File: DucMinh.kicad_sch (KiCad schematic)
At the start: 51 parts, among them J5 USB_B_Micro, J8 Conn_01x04, SW1 SW_Push, U1 STM32F103C8T6, U2 AMS1117-3.3, U3 LM2596SX-5.0/NOPB, U4 TMC2209_SILENTSTEPSTICK, Y1 8 MHz, Y3 32.768 kHz

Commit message: fix routes
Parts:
- removed C11: 10uF, Capacitor_SMD:C_1206_3216Metric_Pad1.33x1.80mm_HandSolder, symbol Device:C
- added C11: 10uf, ul_tantalum6032:tue_tantalum_6032, symbol Device:C_Polarized_US
- R2: footprint Capacitor_SMD:C_0603_1608Metric_Pad1.08x0.95mm_HandSolder -> Resistor_SMD:R_0603_1608Metric_Pad0.98x0.95mm_HandSolder
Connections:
- net +3V3: now also C11.1
- net GND: now also C11.2
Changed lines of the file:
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@@
 	)
 	(symbol
+		(lib_id "Device:C_Polarized_US")
+		(at 127 196.85 0)
+		(unit 1)
+		(exclude_from_sim no)
+		(in_bom yes)
+		(on_board yes)
+		(dnp no)
+		(fields_autoplaced yes)
+		(property "Reference" "C11"
+			(at 130.81 194.9449 0)
+			(effects
+				(font
+					(size 1.27 1.27)
+				)
+				(justify left)
+			)
+		)
+		(property "Value" "10uf"
+			(at 130.81 197.4849 0)
+			(effects
+				(font
+					(size 1.27 1.27)
+				)
+				(justify left)
+			)
+		)
+		(property "Footprint" "ul_tantalum6032:tue_tantalum_6032"
+			(at 127 196.85 0)
+			(effects
+				(font
+					(size 1.27 1.27)
+				)
+				(hide yes)
+			)
+		)
+		(property "Datasheet" "~"
+			(at 127 196.85 0)
+			(effects
+				(font
+					(size 1.27 1.27)
+				)
+				(hide yes)
+			)
+		)
+		(property "Description" "Polarized capacitor, US symbol"
+			(at 127 196.85 0)
+			(effects
+				(font
+					(size 1.27 1.27)
+				)
+				(hide yes)
+			)
+		)
+		(pin "1"
+		)
+		(pin "2"
+		)
+		(instances
+			(project "DucMinh"
+				(path "/e454eeda-a1de-43c9-95d8-58adcb0266a5"
+					(reference "C11")
+					(unit 1)
+				)
+			)
+		)
+	)
+	(symbol
 		(lib_id "power:VDC")
 		(at 220.98 152.4 0)
@@
 	)
 	(symbol
-		(lib_id "Device:C")
-		(at 127 196.85 0)
-		(unit 1)
-		(exclude_from_sim no)
-		(in_bom yes)
-		(on_board yes)
-		(dnp no)
-		(fields_autoplaced yes)
-		(property "Reference" "C11"
-			(at 130.81 195.5799 0)
-			(effects
-				(font
-					(size 1.27 1.27)
-				)
-				(justify left)
-			)
-		)
-		(property "Value" "10uF"
-			(at 130.81 198.1199 0)
-			(effects
-				(font
-					(size 1.27 1.27)
-				)
-				(justify left)
-			)
-		)
-		(property "Footprint" "Capacitor_SMD:C_1206_3216Metric_Pad1.33x1.80mm_HandSolder"
-			(at 127.9652 200.66 0)
-			(effects
-				(font
-					(size 1.27 1.27)
-				)
-				(hide yes)
-			)
-		)
-		(property "Datasheet" "~"
-			(at 127 196.85 0)
-			(effects
-				(font
-					(size 1.27 1.27)
-				)
-				(hide yes)
-			)
-		)
-		(property "Description" "Unpolarized capacitor"
-			(at 127 196.85 0)
-			(effects
-				(font
-					(size 1.27 1.27)
-				)
-				(hide yes)
-			)
-		)
-		(pin "1"
-		)
-		(pin "2"
-		)
-		(instances
-			(project "UART_Half_Duplex"
-				(path "/e454eeda-a1de-43c9-95d8-58adcb0266a5"
-					(reference "C11")
-					(unit 1)
-				)
-			)
-		)
-	)
-	(symbol
 		(lib_id "power:GND")
 		(at 85.09 264.16 270)
@@
 			)
 		)
-		(property "Footprint" "Capacitor_SMD:C_0603_1608Metric_Pad1.08x0.95mm_HandSolder"
+		(property "Footprint" "Resistor_SMD:R_0603_1608Metric_Pad0.98x0.95mm_HandSolder"
 			(at 375.92 83.312 90)
 			(effects

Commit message: .
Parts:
- removed BOOT1: BOOT1, ul_switch-SS12D00:tue_SS12D00_3P_2.5mm, symbol Connector_Generic:Conn_01x03
- removed C15, C16: 10pf, Capacitor_SMD:C_0603_1608Metric_Pad1.08x0.95mm_HandSolder, symbol Device:C
- removed SWD1: SWD, Connector_PinHeader_2.54mm:PinHeader_1x03_P2.54mm_Vertical, symbol Connector_Generic:Conn_01x03
- removed Y3: 32.768 kHz, ul_crytsal_mc306:SOJ_MC-306_EPS, symbol Device:Crystal_GND23
- added STLink_EN1: POWER, Connector_PinHeader_2.54mm:PinHeader_1x02_P2.54mm_Vertical, symbol Connector_Generic:Conn_01x02
- added SWD1: Conn_01x04, Connector_JST:JST_XH_B4B-XH-A_1x04_P2.50mm_Vertical, symbol Connector_Generic:Conn_01x04
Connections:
- net BOOT1 is gone; now on net GND: R7.1
- net +3V3: now also STLink_EN1.1 (Pin_1)
- net GND: now also SWD1.4 (Pin_4)
- net SWD_CLK: now also SWD1.3 (Pin_3)
- net SWD_IO: now also SWD1.2 (Pin_2)
- net 5V_Drive: now reaches PWM1.1-3
- net 5V_Drive: now also PWM1.2-3, PWM1.3-3
- net LSE_OCS_IN: no longer names the net of U1.3 (PC14-OSC32_IN)
- net LSE_OCS_OUT: no longer names the net of U1.4 (PC15-OSC32_OUT)
- new net 3V3_STLINK: STLink_EN1.2 (Pin_2), SWD1.1 (Pin_1)
- no-connect marks 15 -> 10
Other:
- moved on the sheet: C13, C14, R5, R7, R8, TMC_EN1, U1A, Y1

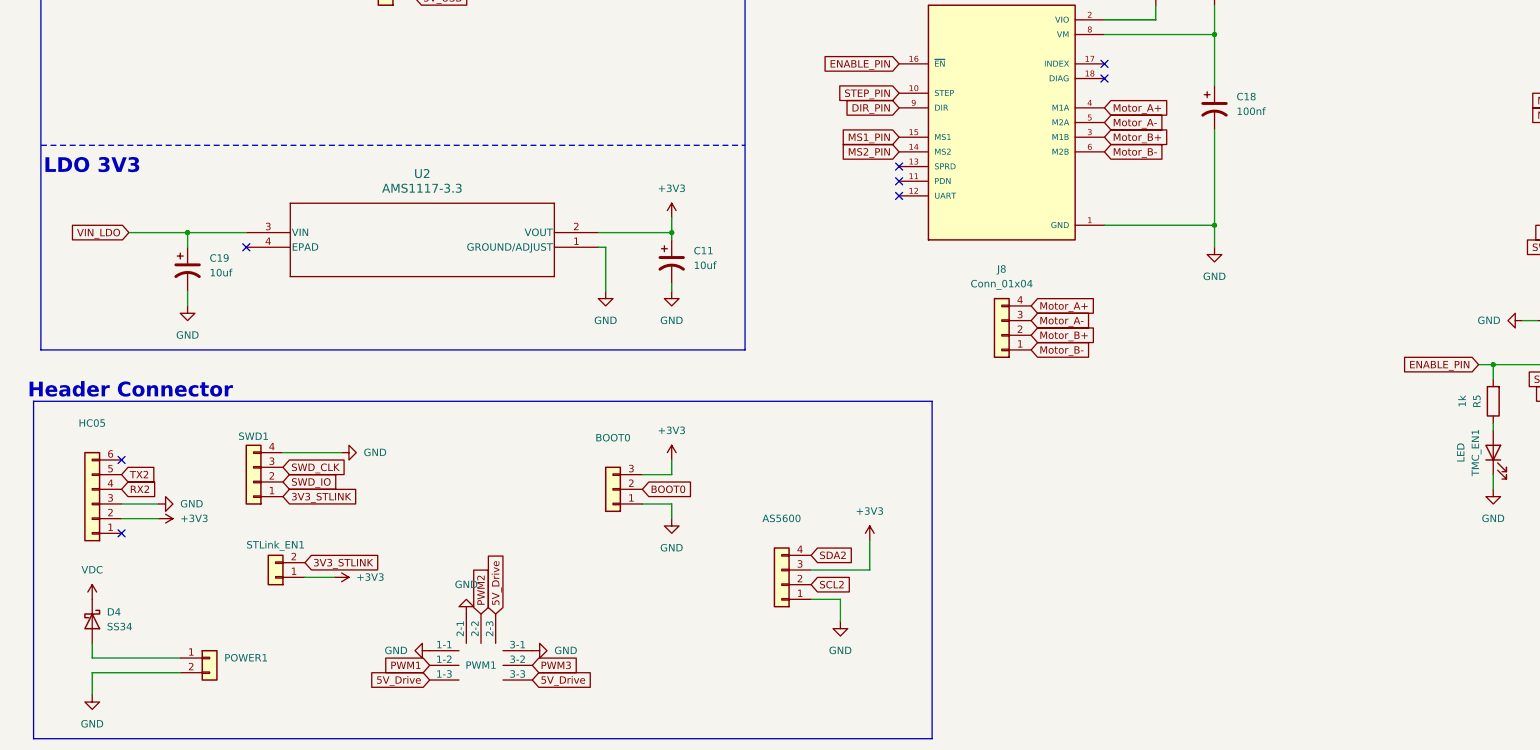
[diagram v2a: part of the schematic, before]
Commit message: add 74hct125 routes
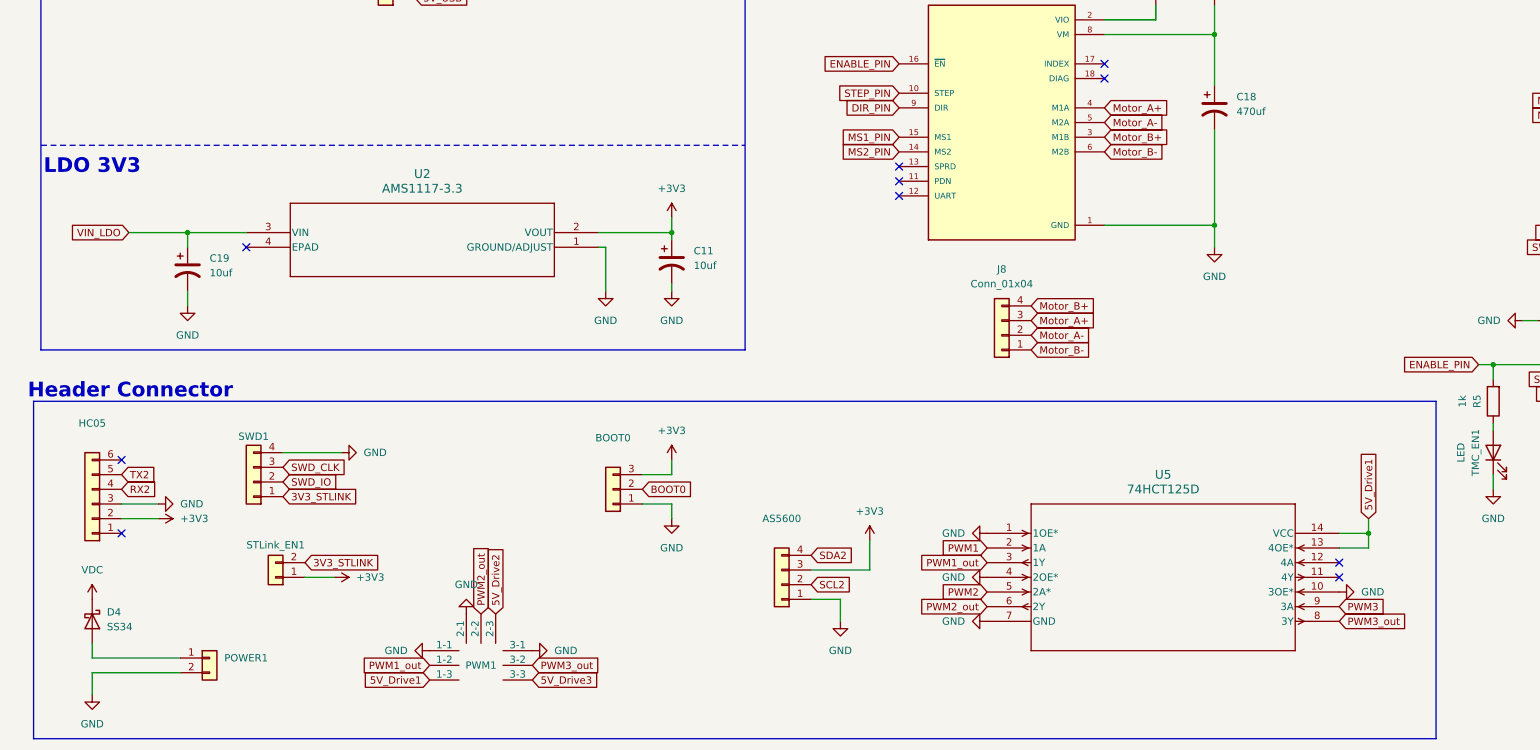
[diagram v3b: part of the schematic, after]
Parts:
- added U5: 74HCT125D, tue_74hct125:SOT108-1_NXP, symbol tue_74hct125d:74HCT125D
- C18: value 100nf -> 470uf
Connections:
- net GND: now also U5.1 (1OE*), U5.10 (3OE*), U5.4 (2OE*), U5.7 (GND)
- net Motor_A+: now also J8.3 (Pin_3); no longer J8.4 (Pin_4)
- net Motor_A-: now also J8.2 (Pin_2); no longer J8.3 (Pin_3)
- net Motor_B+: now also J8.4 (Pin_4); no longer J8.2 (Pin_2)
- net PWM1: now also U5.2 (1A); no longer PWM1.1-2
- net PWM2: now also U5.5 (2A*); no longer PWM1.2-2
- net PWM3: now also U5.9 (3A); no longer PWM1.3-2
- removed net 5V_Drive: PWM1.1-3, PWM1.2-3, PWM1.3-3
- new net 5V_Drive1: PWM1.1-3, U5.13 (4OE*), U5.14 (VCC)
- new net 5V_Drive2: PWM1.2-3
- new net 5V_Drive3: PWM1.3-3
- new net PWM1_out: PWM1.1-2, U5.3 (1Y)
- new net PWM2_out: PWM1.2-2, U5.6 (2Y)
- new net PWM3_out: PWM1.3-2, U5.8 (3Y)
- no-connect marks 10 -> 12

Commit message: add bts7960
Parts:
- removed AS5600: AS5600, Connector_PinHeader_2.54mm:PinHeader_1x04_P2.54mm_Vertical, symbol Connector_Generic:Conn_01x04
- removed BOOT0: BOOT0, ul_switch-SS12D00:tue_SS12D00_3P_2.5mm, symbol Connector_Generic:Conn_01x03
- removed C13: 20pf, Capacitor_SMD:C_0603_1608Metric_Pad1.08x0.95mm_HandSolder, symbol Device:C
- removed C5: 10uf, Capacitor_SMD:C_0603_1608Metric_Pad1.08x0.95mm_HandSolder, symbol Device:C
- removed C8: 1uf, Capacitor_SMD:C_0603_1608Metric_Pad1.08x0.95mm_HandSolder, symbol Device:C
- removed HC05: HC05, Connector_PinHeader_2.54mm:PinHeader_1x06_P2.54mm_Vertical, symbol Connector_Generic:Conn_01x06
- removed PC13, PWR1, TMC_EN1: LED, LED_SMD:LED_0603_1608Metric_Pad1.05x0.95mm_HandSolder, symbol Device:LED
- removed POWER1: POWER, ul_TerminalBlock:TerminalBlock_bornier-2_P5.08mm, symbol Connector_Generic:Conn_01x02
- removed PWM1: ~, ul_Conn_03x03:tue_conn_03x03_2.54mm, symbol Conn_03x03:Conn_03x03
- removed R2, R4, R5: 1k, Resistor_SMD:R_0603_1608Metric_Pad0.98x0.95mm_HandSolder, symbol Device:R
- removed R8: 10k, Resistor_SMD:R_0603_1608Metric_Pad0.98x0.95mm_HandSolder, symbol Device:R
- removed STLink_EN1: POWER, Connector_PinHeader_2.54mm:PinHeader_1x02_P2.54mm_Vertical, symbol Connector_Generic:Conn_01x02
- removed SWD1: Conn_01x04, Connector_JST:JST_XH_B4B-XH-A_1x04_P2.50mm_Vertical, symbol Connector_Generic:Conn_01x04
- removed U1: STM32F103C8T6, ul_stm32:LQFP48_STM, symbol ul_STM32F103C8T6:STM32F103C8T6
- removed U5: 74HCT125D, tue_74hct125:SOT108-1_NXP, symbol tue_74hct125d:74HCT125D
- removed VIN1: Conn_01x03, ul_switch-SS12D00:tue_SS12D00_3P_2.5mm, symbol Connector_Generic:Conn_01x03
- added C11, C12, C13: 330uf, Capacitor_THT:CP_Radial_D8.0mm_P5.00mm, symbol Device:C_Polarized_US
- added C15: 20pf, Capacitor_SMD:C_0603_1608Metric_Pad1.08x0.95mm_HandSolder, symbol Device:C
- added DS1: LED_PWR, LED_SMD:LED_0603_1608Metric_Pad1.05x0.95mm_HandSolder, symbol Device:LED
- added DS2: LED_PC13, LED_SMD:LED_0603_1608Metric_Pad1.05x0.95mm_HandSolder, symbol Device:LED
- added DS4: LED_TMC_EN, LED_SMD:LED_0603_1608Metric_Pad1.05x0.95mm_HandSolder, symbol Device:LED
- added J1: Power, tue_TerminalBlock:TerminalBlock_bornier-2_P5.08mm, symbol Connector_Generic:Conn_01x02
- added J10: HC05, Connector_PinHeader_2.54mm:PinHeader_1x06_P2.54mm_Vertical, symbol Connector_Generic:Conn_01x06
- added J11: PWR_Selection, tue_switch-SS12D00:tue_SS12D00_3P_2.5mm, symbol Connector_Generic:Conn_01x03
- added J12: BOOT0, tue_switch-SS12D00:tue_SS12D00_3P_2.5mm, symbol Connector_Generic:Conn_01x03
- added J2: M1, tue_TerminalBlock:TerminalBlock_bornier-2_P5.08mm, symbol Connector_Generic:Conn_01x02
- added J4: M2, tue_TerminalBlock:TerminalBlock_bornier-2_P5.08mm, symbol Connector_Generic:Conn_01x02
- added J5: M3, tue_TerminalBlock:TerminalBlock_bornier-2_P5.08mm, symbol Connector_Generic:Conn_01x02
- added J6: AS5600, Connector_PinHeader_2.54mm:PinHeader_1x04_P2.54mm_Vertical, symbol Connector_Generic:Conn_01x04
- added J7: STLink, Connector_PinHeader_2.54mm:PinHeader_1x04_P2.54mm_Vertical, symbol Connector_Generic:Conn_01x04
- added J9: STLink_EN, Connector_PinHeader_2.54mm:PinHeader_1x02_P2.54mm_Vertical, symbol Connector_Generic:Conn_01x02
- added R10, R12, R19, R20, R22, R24, R26, R28, R29, R30, R31, R32, R33, R9: 10k, Resistor_SMD:R_0603_1608Metric_Pad0.98x0.95mm_HandSolder, symbol Device:R
- added R13, R16: 1k, Resistor_SMD:R_0603_1608Metric_Pad0.98x0.95mm_HandSolder, symbol Device:R
- added U10, U5, U8: BTS7960B, tue_bts7960b:DPAK127P1490X440-8N, symbol tue_bts7960:BTS7960B
- added U6: STM32F103RCT6, tue_stm32f103rct6:QFP50P1200X1200X160-64N, symbol tue_f103rct6:STM32F103RCT6
- C10: renamed from C11; footprint ul_tantalum6032:tue_tantalum_6032 -> tue_tantalum6032:tue_tantalum_6032
- C18: renamed from C19; footprint ul_tantalum6032:tue_tantalum_6032 -> tue_tantalum6032:tue_tantalum_6032
- J3: renamed from J5; footprint ul_USB:USB_Micro-B_Wuerth-629105150521 -> Connector_USB:USB_Micro-B_Amphenol_10118193-0001LF_Horizontal
- J8: value Conn_01x04 -> Stepper_Motor
- L1: footprint ul_inductor_smd:tue__CDRH127LDNP-470MC_SUM -> tue_inductor_smd:tue__CDRH127LDNP-470MC_SUM
- R7: value 10k -> 1k
- U2: footprint ul_ams1117:SOT_AMS_ADS -> tue_ams1117:SOT_AMS_ADS
- U3: footprint ul_lm2596hvs:tue_lm2596 -> tue_lm2596hvs:tue_lm2596
- U4: footprint ul_TMC2209:tue_TMC2209 -> tue_TMC2209:tue_TMC2209
- renumbered C17 to C16, C18 to C17, C6 to C5, C7 to C6, C9 to C8, C10 to C9, D3 to D1, D4 to D2
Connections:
- net +3V3: now also C5.1, C6.1, R7.2, J10.2 (Pin_2), J12.3 (Pin_3), J6.3 (Pin_3), J9.1 (Pin_1), R16.1, U6.1 (VBAT), U6.19 (VDD_4), U6.32 (VDD_1), U6.48 (VDD_2), U6.64 (VDD_3)
- net 3V3_STLINK: now also J7.1 (Pin_1), J9.2 (Pin_2)
- net 5V_LDO: now also J11.3 (Pin_3)
- net 5V_USB: now also J11.1 (Pin_1)
- net BOOT0: now also R9.1, U6.60 (BOOT0)
- net ENABLE_PIN: now also R13.2
- net GND: now also C11.2, C12.2, C13.2, C15.2, DS1.1 (K), DS4.1 (K), J1.1 (Pin_1), J10.3 (Pin_3), J12.1 (Pin_1), J2.1 (Pin_1), J4.1 (Pin_1), J5.1 (Pin_1), J6.1 (Pin_1), J7.4 (Pin_4), R10.1, R12.1, R19.1, R20.1, R22.2, R24.1, R26.2, U10.1 (GND), U5.1 (GND), U6.12 (VSSA), U6.18 (VSS_4), U6.31 (VSS_1), U6.47 (VSS_2), U6.63 (VSS_3), U8.1 (GND); no longer R7.1
- net PC13_LED: now also DS2.1 (K), U6.2 (PC13-TAMPER-RTC)
- net PWM1: now also R28.1
- net PWM2: now also R30.1
- net PWM3: now also R32.1
- net RESET: now also U6.7 (NRST)
- net RX2: now also J10.4 (Pin_4)
- net SCL2: now also J6.2 (Pin_2)
- net SDA2: now also J6.4 (Pin_4)
- net SWD_CLK: now also J7.3 (Pin_3), U6.49 (PA14)
- net SWD_IO: now also J7.2 (Pin_2), U6.46 (PA13)
- net TX2: now also J10.5 (Pin_5)
- net USB+: now also U6.45 (PA12)
- net USB-: now also U6.44 (PA11)
- net VDC: now also C11.1, C12.1, C13.1, U10.7 (VS), U5.7 (VS), U8.7 (VS)
- net VIN_LDO: now also J11.2 (Pin_2)
- net at D2.2 (A): now also J1.2 (Pin_2)
- net HSE_OCS_IN: no longer names the net of Y1.1
- net HSE_OCS_IN: now also C14.1, U6.6 (PD1_OSC_OUT)
- net HSE_OCS_OUT: no longer names the net of Y1.2
- net HSE_OCS_OUT: now also C15.1, U6.5 (PD0-OSC_IN); no longer C14.1
- new net: DS2.2 (A), R16.2
- new net: J12.2 (Pin_2), R9.2
- new net: R19.2, U5.6 (IS)
- new net: R29.2, U5.3 (INH)
- new net: R12.2, U5.5 (SR)
- new net: DS4.2 (A), R13.1
- new net: R22.1, U8.6 (IS)
- new net: R28.2, U5.2 (IN)
- new net: R32.2, U8.2 (IN)
- new net: R30.2, U10.2 (IN)
- new net: R31.2, U10.3 (INH)
- new net: R26.1, U10.6 (IS)
- new net: R20.2, U8.5 (SR)
- new net: R33.2, U8.3 (INH)
- new net: DS1.2 (A), R7.1
- new net: R24.2, U10.5 (SR)
- new net BOOT1: R10.2, U6.28 (PB2)
- new net M1+: J2.2 (Pin_2), U5.4 (OUT), U5.8 (OUT)
- new net M1_EN: R29.1
- new net M2+: J4.2 (Pin_2), U10.4 (OUT), U10.8 (OUT)
- new net M2_EN: R31.1
- new net M3+: J5.2 (Pin_2), U8.4 (OUT), U8.8 (OUT)
- new net M3_EN: R33.1
- new net VDDA: FB1.1, U6.13 (VDDA)
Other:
- note added: "1. Buck 24V -> 5V 2. LDO 5V -> 3V3 3. TMC2209 4. MOSFET for DC Motor 5. Pinout (Debug, Boot 0-1 , 6 PWM pin for DC motor , 1 PWM pin for Stepper motor , 1 IO pin for Stepper motor , HC-05 pin)"
- note added: "DC MOTOR - MOSFET"
- note added: "DECOUPLING"
- note added: "LED"
- note added: "RESET"
- note added: "STEPPER"
- note removed: "1. Buck 24V -> 5V 2. LDO 5V -> 3V3 3. TMC2209 4. Pinout (Debug, Boot 0-1, 3 PWM pin, HC-05 pin)"
- note removed: "Crystal"
- note removed: "Decoupling"
- note removed: "Power 5V Selection"
- note removed: "Reset Button"
- moved on the sheet: C1, C10, C16, C17, C18, C2, C3, C4, C5, C6, C8, C9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

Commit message: final
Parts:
- removed J9: STLink_EN, Connector_PinHeader_2.54mm:PinHeader_1x02_P2.54mm_Vertical, symbol Connector_Generic:Conn_01x02
- removed R29, R31, R33: 10k, Resistor_SMD:R_0603_1608Metric_Pad0.98x0.95mm_HandSolder, symbol Device:R
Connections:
- net +3V3: now also U10.3 (INH), U5.3 (INH), U8.3 (INH)
- net DIR_PIN: now also U6.33 (PB12)
- net ENABLE_PIN: now also U6.37 (PC6)
- net MS1_PIN: now also U6.36 (PB15)
- net MS2_PIN: now also U6.35 (PB14)
- net PWM1: now also U6.55 (PB3)
- net PWM2: now also U6.56 (PB4)
- net PWM3: now also U6.57 (PB5)
- net RX2: now also U6.30 (PB11)
- net SCL2: now also U6.58 (PB6)
- net SDA2: now also U6.59 (PB7)
- net STEP_PIN: now also U6.34 (PB13)
- net TX2: now also U6.29 (PB10)
- net 3V3_STLINK: no longer names the net of J7.1 (Pin_1)
- no-connect marks 12 -> 13
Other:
- moved on the sheet: C9, R3, SW1

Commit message: final2
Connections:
- net DIR_PIN: now also U6.39 (PC8); no longer U6.33 (PB12)
- net ENABLE_PIN: now also U6.43 (PA10); no longer U6.37 (PC6)
- net MS1_PIN: now also U6.42 (PA9); no longer U6.36 (PB15)
- net MS2_PIN: now also U6.41 (PA8); no longer U6.35 (PB14)
- net STEP_PIN: now also U6.40 (PC9); no longer U6.34 (PB13)
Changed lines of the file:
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@@
 	(global_label "DIR_PIN"
 		(shape input)
-		(at 283.21 198.12 180)
-		(fields_autoplaced yes)
-		(effects
-			(font
-				(size 1.27 1.27)
-			)
-			(justify right)
-		)
-		(property "Intersheetrefs" "${INTERSHEET_REFS}"
-			(at 272.9071 198.12 0)
-			(effects
-				(font
-					(size 1.27 1.27)
-				)
-				(justify right)
+		(at 344.17 170.18 0)
+		(fields_autoplaced yes)
+		(effects
+			(font
+				(size 1.27 1.27)
+			)
+			(justify left)
+		)
+		(property "Intersheetrefs" "${INTERSHEET_REFS}"
+			(at 354.4729 170.18 0)
+			(effects
+				(font
+					(size 1.27 1.27)
+				)
+				(justify left)
 				(hide yes)
 			)
@@
 	(global_label "STEP_PIN"
 		(shape input)
-		(at 283.21 200.66 180)
-		(fields_autoplaced yes)
-		(effects
-			(font
-				(size 1.27 1.27)
-			)
-			(justify right)
-		)
-		(property "Intersheetrefs" "${INTERSHEET_REFS}"
-			(at 271.4558 200.66 0)
-			(effects
-				(font
-					(size 1.27 1.27)
-				)
-				(justify right)
+		(at 344.17 172.72 0)
+		(fields_autoplaced yes)
+		(effects
+			(font
+				(size 1.27 1.27)
+			)
+			(justify left)
+		)
+		(property "Intersheetrefs" "${INTERSHEET_REFS}"
+			(at 355.9242 172.72 0)
+			(effects
+				(font
+					(size 1.27 1.27)
+				)
+				(justify left)
 				(hide yes)
 			)
@@
 	(global_label "ENABLE_PIN"
 		(shape input)
-		(at 344.17 165.1 0)
-		(fields_autoplaced yes)
-		(effects
-			(font
-				(size 1.27 1.27)
-			)
-			(justify left)
-		)
-		(property "Intersheetrefs" "${INTERSHEET_REFS}"
-			(at 358.3433 165.1 0)
-			(effects
-				(font
-					(size 1.27 1.27)
-				)
-				(justify left)
+		(at 283.21 149.86 180)
+		(fields_autoplaced yes)
+		(effects
+			(font
+				(size 1.27 1.27)
+			)
+			(justify right)
+		)
+		(property "Intersheetrefs" "${INTERSHEET_REFS}"
+			(at 269.0367 149.86 0)
+			(effects
+				(font
+					(size 1.27 1.27)
+				)
+				(justify right)
 				(hide yes)
 			)
@@
 	(global_label "MS2_PIN"
 		(shape input)
-		(at 283.21 203.2 180)
-		(fields_autoplaced yes)
-		(effects
-			(font
-				(size 1.27 1.27)
-			)
-			(justify right)
-		)
-		(property "Intersheetrefs" "${INTERSHEET_REFS}"
-			(at 272.1815 203.2 0)
+		(at 283.21 144.78 180)
+		(fields_autoplaced yes)
+		(effects
+			(font
+				(size 1.27 1.27)
+			)
+			(justify right)
+		)
+		(property "Intersheetrefs" "${INTERSHEET_REFS}"
+			(at 272.1815 144.78 0)
 			(effects
 				(font
@@
 	(global_label "MS1_PIN"
 		(shape input)
-		(at 283.21 205.74 180)
-		(fields_autoplaced yes)
-		(effects
-			(font
-				(size 1.27 1.27)
-			)
-			(justify right)
-		)
-		(property "Intersheetrefs" "${INTERSHEET_REFS}"
-			(at 272.1815 205.74 0)
-			(effects
-				(font
+		(at 283.21 147.32 180)
+		(fields_autoplaced yes)
+		(effects
+			(font
+				(size 1.27 1.27)
+			)
+			(justify right)
+		)
+		(property "Intersheetrefs" "${INTERSHEET_REFS}"
+			(at 272.1815 147.32 0)
+			(effects
+				(font
